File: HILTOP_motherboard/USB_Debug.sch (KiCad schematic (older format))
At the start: 16 parts, among them U40 SP3003-02XJ, U41 CP2102N-A01-GQFN24

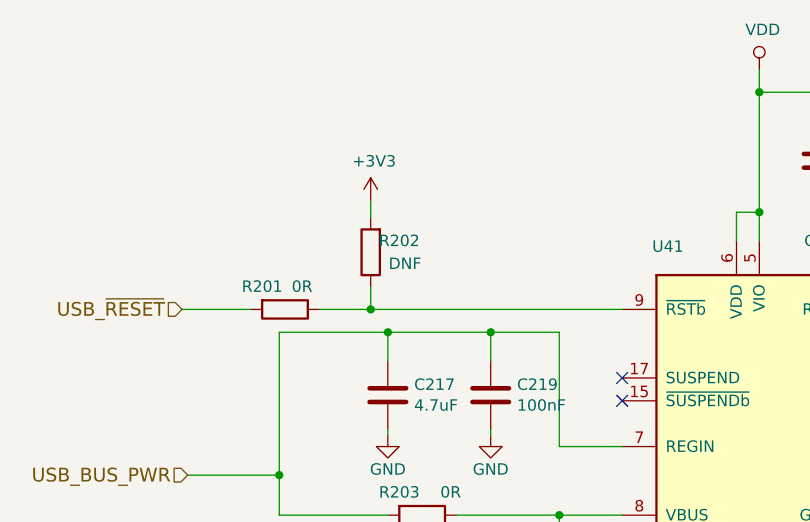
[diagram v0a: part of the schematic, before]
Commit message: Moved Backplane Connctor 2mm to the left to fix alignment issue on HILTOP 63HP
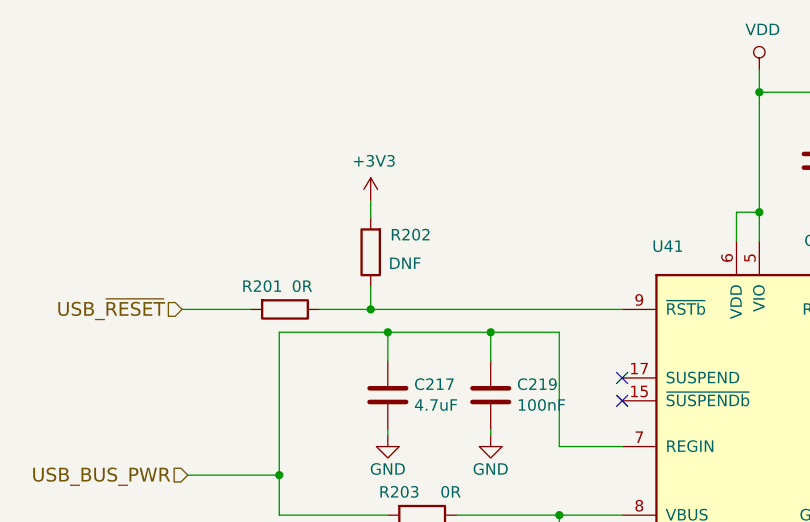
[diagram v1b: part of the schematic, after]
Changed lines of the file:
@@
 EESchema Schematic File Version 4
-LIBS:HILTOP_Motherboard-cache
-EELAYER 29 0
+EELAYER 30 0
 EELAYER END
 $Descr A4 11693 8268
@@
 Sheet 9 12
 Title "HILTOP Motherboard"
-Date "2019-07-03"
-Rev "Rev B"
+Date "2020-04-28"
+Rev "Rev C"
 Comp "Devtank Ltd"
 Comment1 ""
@@
 U 1 1 5C3C0F83
 P 3825 2625
-F 0 "R202" H 3700 2575 50  0000 C CNN
+F 0 "R202" H 3650 2550 50  0000 C CNN
 F 1 "DNF" H 3675 2675 50  0000 C CNN
 F 2 "Resistor_SMD:R_0603_1608Metric" V 3755 2625 50  0001 C CNN

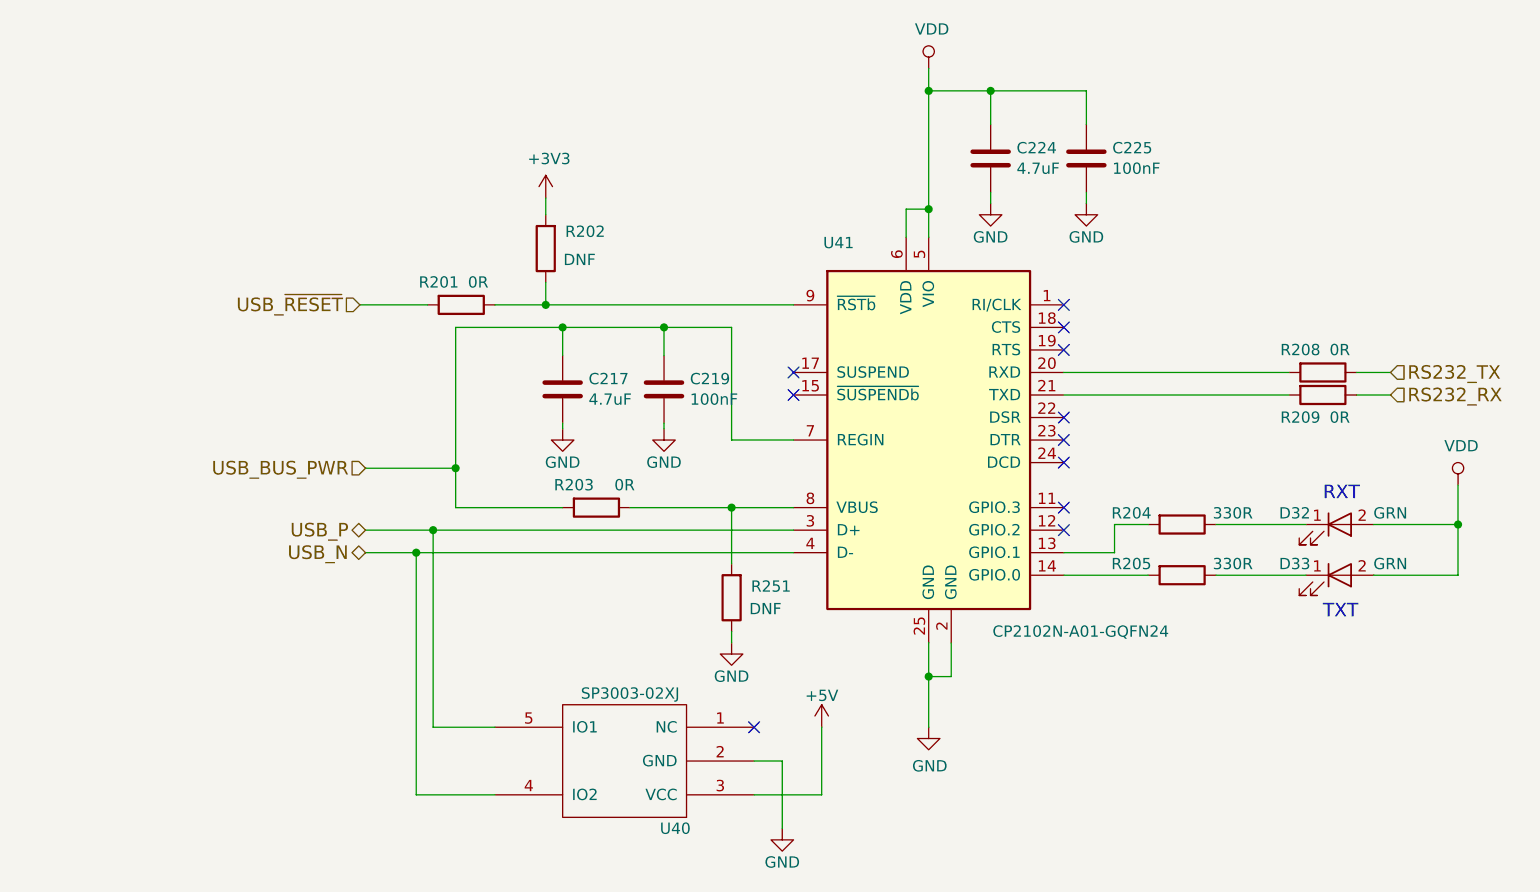
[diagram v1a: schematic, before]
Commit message: added small fixes for USB Debug chip to allow independant power up from external cable
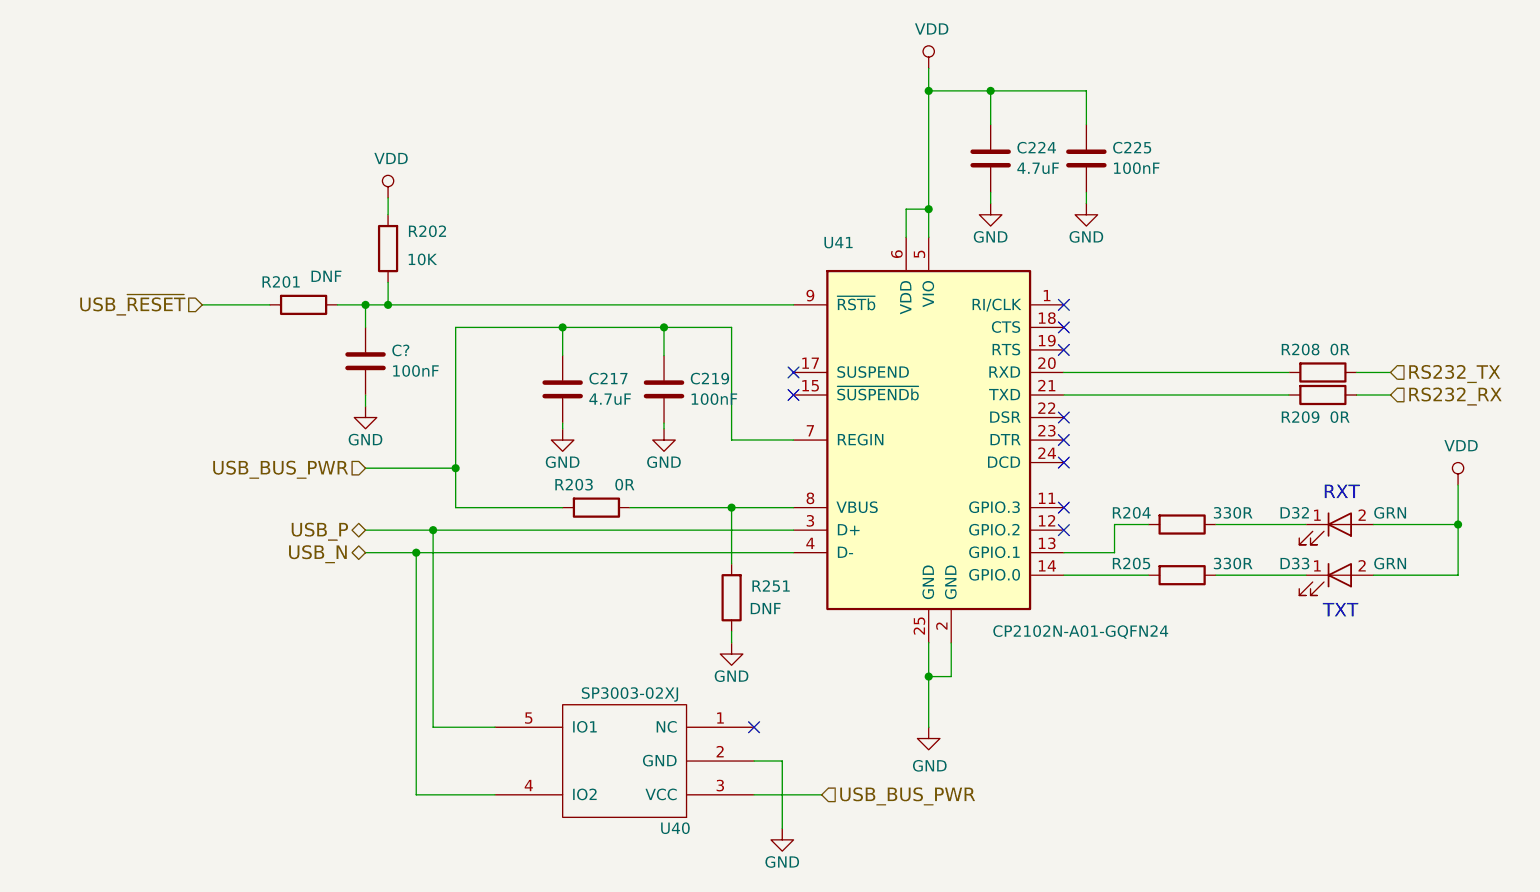
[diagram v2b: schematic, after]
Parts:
- added C?: 100nF, Capacitor_SMD:C_0603_1608Metric, symbol HILTOP_Motherboard-rescue:C-device
- R201: value 0R -> DNF
- R202: value DNF -> 10K; Devtank (none) -> 101-010
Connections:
- net +3V3 is gone; now on net VDD: R202.2
- net +5V is gone; now on net USB_BUS_PWR: U40.3 (VCC)
- net GND: now also C?.2
- net at R201.1, R202.1, U41.9 (~RSTb): now also C?.1
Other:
- moved on the sheet: R201, R202
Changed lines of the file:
@@
 Wire Wire Line
 	3425 3775 3900 3775
-Text HLabel 3000 2875 0    60   Input ~ 0
+Text HLabel 2300 2875 0    60   Input ~ 0
 USB_~RESET
 Wire Wire Line
-	3000 2875 3300 2875
+	2300 2875 2600 2875
 $Comp
 L HILTOP_Motherboard-rescue:R-device R?
@@
 L HILTOP_Motherboard-rescue:R-device R201
 U 1 1 5C3C0EE1
-P 3450 2875
-F 0 "R201" V 3350 2775 50  0000 C CNN
-F 1 "0R" V 3350 2950 50  0000 C CNN
-F 2 "Resistor_SMD:R_0603_1608Metric" V 3380 2875 50  0001 C CNN
-F 3 "" H 3450 2875 50  0001 C CNN
-F 4 "101-005" V 3450 2875 50  0001 C CNN "Devtank"
-	1    3450 2875
+P 2750 2875
+F 0 "R201" V 2650 2775 50  0000 C CNN
+F 1 "DNF" V 2625 2975 50  0000 C CNN
+F 2 "Resistor_SMD:R_0603_1608Metric" V 2680 2875 50  0001 C CNN
+F 3 "" H 2750 2875 50  0001 C CNN
+F 4 "101-005" V 2750 2875 50  0001 C CNN "Devtank"
+	1    2750 2875
 	0    1    1    0
 $EndComp
 Wire Wire Line
-	3600 2875 3825 2875
+	2900 2875 3025 2875
 $Comp
 L HILTOP_Motherboard-rescue:R-device R202
 U 1 1 5C3C0F83
-P 3825 2625
-F 0 "R202" H 3650 2550 50  0000 C CNN
-F 1 "DNF" H 3675 2675 50  0000 C CNN
-F 2 "Resistor_SMD:R_0603_1608Metric" V 3755 2625 50  0001 C CNN
-F 3 "" H 3825 2625 50  0001 C CNN
-	1    3825 2625
+P 3125 2625
+F 0 "R202" H 2950 2550 50  0000 C CNN
+F 1 "10K" H 2975 2675 50  0000 C CNN
+F 2 "Resistor_SMD:R_0603_1608Metric" V 3055 2625 50  0001 C CNN
+F 3 "" H 3125 2625 50  0001 C CNN
+F 4 "101-010" H 3125 2625 50  0001 C CNN "Devtank"
+	1    3125 2625
 	-1   0    0    1
 $EndComp
 Wire Wire Line
-	3825 2775 3825 2875
-Connection ~ 3825 2875
-Wire Wire Line
-	3825 2875 4925 2875
-$Comp
-L power:+3V3 #PWR0218
-U 1 1 5C3C1B45
-P 3825 2400
-F 0 "#PWR0218" H 3825 2250 50  0001 C CNN
-F 1 "+3V3" H 3840 2573 50  0000 C CNN
-F 2 "" H 3825 2400 50  0001 C CNN
-F 3 "" H 3825 2400 50  0001 C CNN
-	1    3825 2400
-	1    0    0    -1
-$EndComp
-Wire Wire Line
-	3825 2400 3825 2475
+	3125 2775 3125 2875
+Connection ~ 3125 2875
+Wire Wire Line
+	3125 2400 3125 2475
 $Comp
 L HILTOP_Motherboard-rescue:C-device C224
@@
 	4875 5200 4875 4900
 Wire Wire Line
-	5050 5050 5050 4750
-Wire Wire Line
 	4750 5050 5050 5050
 $Comp
@@
 F 3 "" H 4875 5200 50  0000 C CNN
 	1    4875 5200
-	1    0    0    -1
-$EndComp
-$Comp
-L power:+5V #PWR?
-U 1 1 5C3985EC
-P 5050 4750
-AR Path="/589A1B39/5C3985EC" Ref="#PWR?"  Part="1"
-AR Path="/5AFBC859/5C3985EC" Ref="#PWR0222"  Part="1"
-F 0 "#PWR0222" H 5050 4600 50  0001 C CNN
-F 1 "+5V" H 5050 4890 50  0000 C CNN
-F 2 "" H 5050 4750 50  0000 C CNN
-F 3 "" H 5050 4750 50  0000 C CNN
-	1    5050 4750
 	1    0    0    -1
 $EndComp
@@
 Wire Wire Line
 	5525 1825 5525 1925
+$Comp
+L power:VDD #PWR?
+U 1 1 605C5451
+P 3125 2400
+F 0 "#PWR?" H 3125 2250 50  0001 C CNN
+F 1 "VDD" H 3140 2573 50  0000 C CNN
+F 2 "" H 3125 2400 50  0001 C CNN
+F 3 "" H 3125 2400 50  0001 C CNN
+	1    3125 2400
+	1    0    0    -1
+$EndComp
+Text HLabel 5050 5050 2    60   Input ~ 0
+USB_BUS_PWR
+Wire Wire Line
+	3125 2875 4925 2875
+$Comp
+L HILTOP_Motherboard-rescue:C-device C?
+U 1 1 605DF810
+P 3025 3125
+AR Path="/5AFBC859/605DF810" Ref="C?"  Part="1"
+AR Path="/5A951BF0/605DF810" Ref="C?"  Part="1"
+F 0 "C?" H 3140 3171 50  0000 L CNN
+F 1 "100nF" H 3140 3080 50  0000 L CNN
+F 2 "Capacitor_SMD:C_0603_1608Metric" H 3063 2975 50  0001 C CNN
+F 3 "" H 3025 3125 50  0001 C CNN
+F 4 "105-002" H 3025 3125 50  0001 C CNN "Devtank"
+	1    3025 3125
+	1    0    0    -1
+$EndComp
+Wire Wire Line
+	3025 2975 3025 2875
+Connection ~ 3025 2875
+Wire Wire Line
+	3025 2875 3125 2875
+$Comp
+L power:GND #PWR?
+U 1 1 605E1FA8
+P 3025 3325
+F 0 "#PWR?" H 3025 3075 50  0001 C CNN
+F 1 "GND" H 3025 3175 50  0000 C CNN
+F 2 "" H 3025 3325 50  0001 C CNN
+F 3 "" H 3025 3325 50  0001 C CNN
+	1    3025 3325
+	1    0    0    -1
+$EndComp
+Wire Wire Line
+	3025 3275 3025 3325
 $EndSCHEMATC

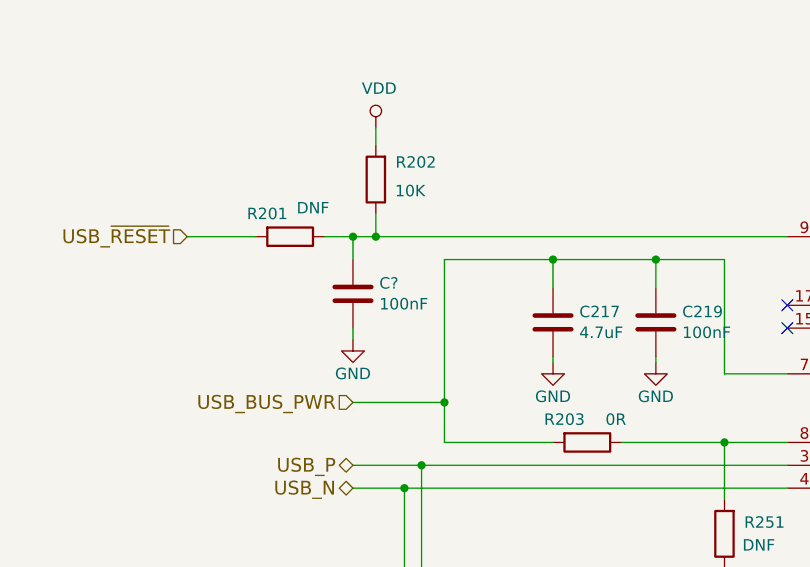
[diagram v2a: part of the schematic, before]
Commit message: updates to include - license, remove U46, swap crystal Y1
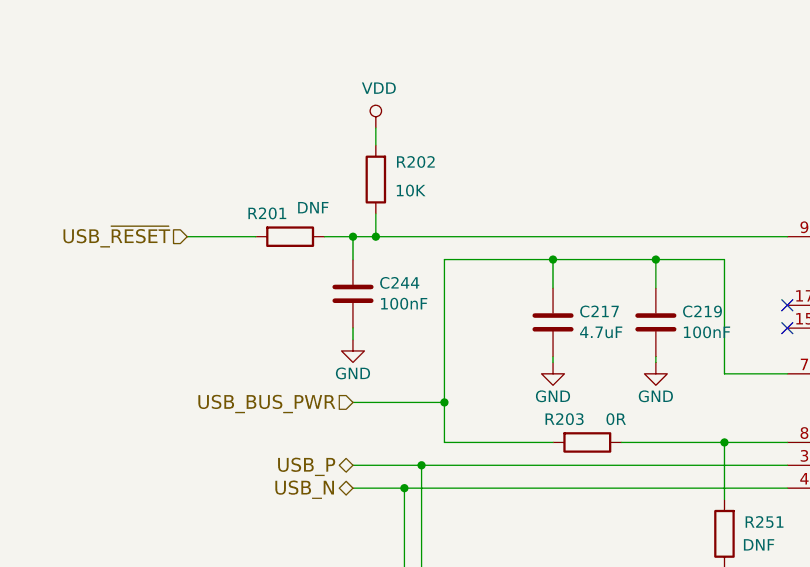
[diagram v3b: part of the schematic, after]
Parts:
- gave numbers to parts that had none: 1
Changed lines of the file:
@@
 	5525 1825 5525 1925
 $Comp
-L power:VDD #PWR?
+L power:VDD #PWR0218
 U 1 1 605C5451
 P 3125 2400
-F 0 "#PWR?" H 3125 2250 50  0001 C CNN
+F 0 "#PWR0218" H 3125 2250 50  0001 C CNN
 F 1 "VDD" H 3140 2573 50  0000 C CNN
 F 2 "" H 3125 2400 50  0001 C CNN
@@
 	3125 2875 4925 2875
 $Comp
-L HILTOP_Motherboard-rescue:C-device C?
+L HILTOP_Motherboard-rescue:C-device C244
 U 1 1 605DF810
 P 3025 3125
-AR Path="/5AFBC859/605DF810" Ref="C?"  Part="1"
+AR Path="/5AFBC859/605DF810" Ref="C244"  Part="1"
 AR Path="/5A951BF0/605DF810" Ref="C?"  Part="1"
-F 0 "C?" H 3140 3171 50  0000 L CNN
+F 0 "C244" H 3140 3171 50  0000 L CNN
 F 1 "100nF" H 3140 3080 50  0000 L CNN
 F 2 "Capacitor_SMD:C_0603_1608Metric" H 3063 2975 50  0001 C CNN
@@
 	3025 2875 3125 2875
 $Comp
-L power:GND #PWR?
+L power:GND #PWR0222
 U 1 1 605E1FA8
 P 3025 3325
-F 0 "#PWR?" H 3025 3075 50  0001 C CNN
+F 0 "#PWR0222" H 3025 3075 50  0001 C CNN
 F 1 "GND" H 3025 3175 50  0000 C CNN
 F 2 "" H 3025 3325 50  0001 C CNN

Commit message: changed silkscreen to revD and updated sheet information
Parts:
- U40: symbol Devtank:SP3003-02XJ -> HILTOP_Motherboard-rescue:SP3003-02XJ-Devtank
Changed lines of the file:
@@
 Sheet 9 12
 Title "HILTOP Motherboard"
-Date "2020-04-28"
-Rev "Rev C"
+Date "2021-02-17"
+Rev "Rev D"
 Comp "Devtank Ltd"
-Comment1 ""
+Comment1 "Part No: 304-001"
 Comment2 ""
 Comment3 ""
@@
 $EndComp
 $Comp
-L Devtank:SP3003-02XJ U?
+L HILTOP_Motherboard-rescue:SP3003-02XJ-Devtank U?
 U 1 1 5C3985E5
 P 4000 4900
